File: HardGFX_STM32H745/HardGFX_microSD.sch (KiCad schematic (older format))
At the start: 8 parts, among them J10 PJS008-2003-1

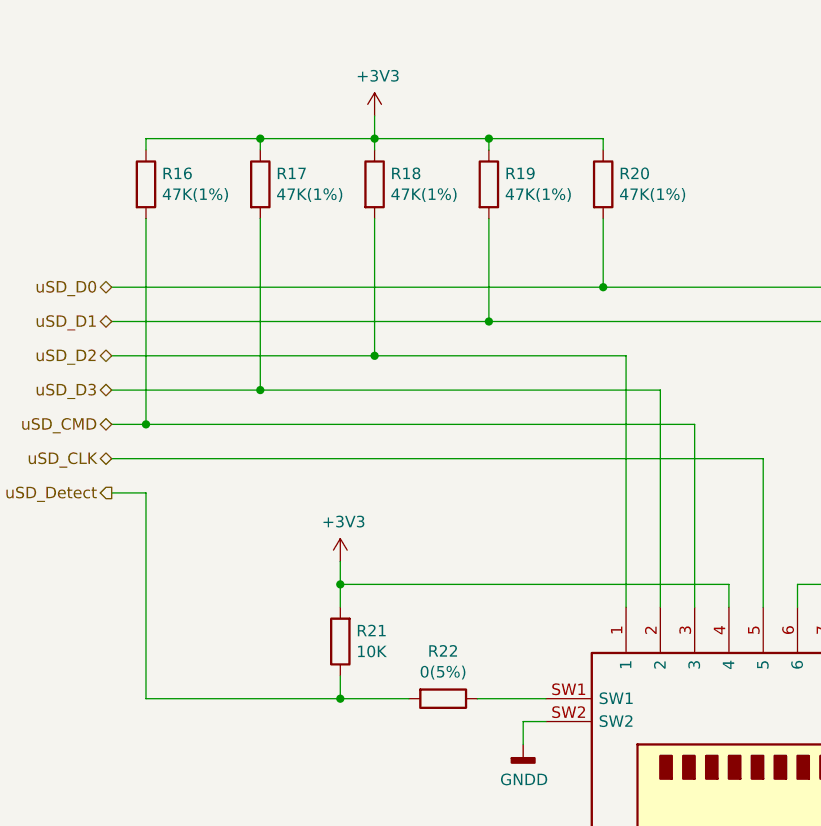
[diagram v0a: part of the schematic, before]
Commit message: Filling field for do BOM with Kicost  and create proyect on IDE to start setting peripheral in MCU
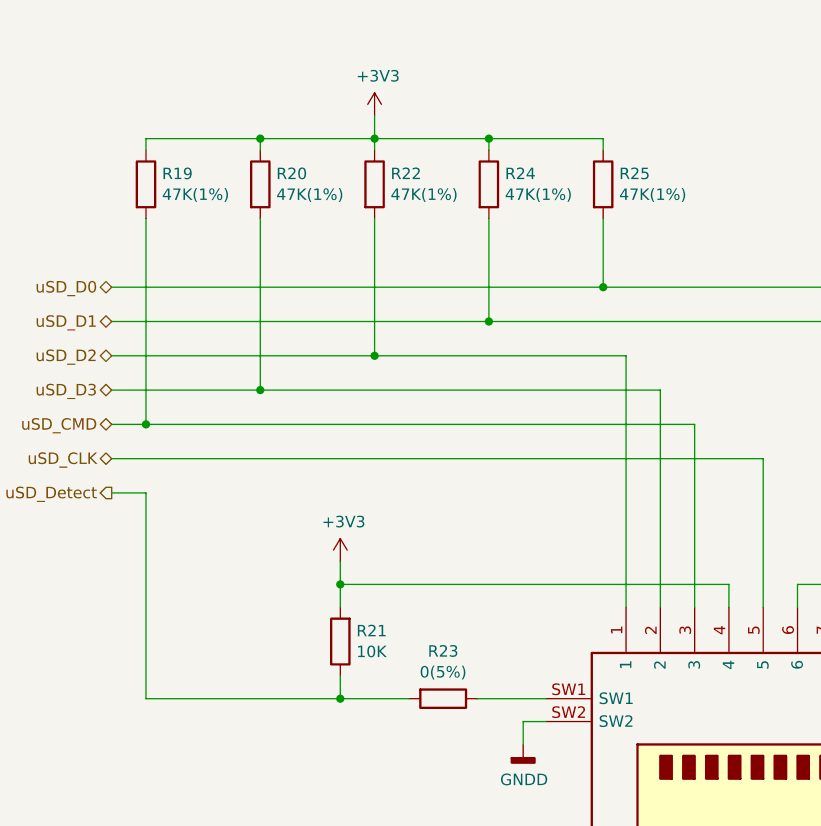
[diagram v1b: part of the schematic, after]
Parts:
- renumbered R16 to R19, R17 to R20, R18 to R22, R22 to R23, R19 to R24, R20 to R25
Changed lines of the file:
@@
 $EndComp
 $Comp
-L power:GNDD #PWR068
+L power:GNDD #PWR080
 U 1 1 60F78B55
 P 5100 6150
-F 0 "#PWR068" H 5100 5900 50  0001 C CNN
+F 0 "#PWR080" H 5100 5900 50  0001 C CNN
 F 1 "GNDD" H 5104 5995 50  0000 C CNN
 F 2 "" H 5100 6150 50  0001 C CNN
@@
 	5100 6050 5100 6150
 $Comp
-L power:GNDD #PWR067
+L power:GNDD #PWR079
 U 1 1 60F79B74
 P 3100 5700
-F 0 "#PWR067" H 3100 5450 50  0001 C CNN
+F 0 "#PWR079" H 3100 5450 50  0001 C CNN
 F 1 "GNDD" H 3104 5545 50  0000 C CNN
 F 2 "" H 3100 5700 50  0001 C CNN
@@
 uSD_D3
 $Comp
-L Device:R R22
+L Device:R R23
 U 1 1 60F7C1AA
 P 2750 5500
-F 0 "R22" V 2543 5500 50  0000 C CNN
+F 0 "R23" V 2543 5500 50  0000 C CNN
 F 1 "0(5%)" V 2634 5500 50  0000 C CNN
 F 2 "" V 2680 5500 50  0001 C CNN
@@
 $EndComp
 $Comp
-L power:+3V3 #PWR065
+L power:+3V3 #PWR077
 U 1 1 60F7DC6F
 P 2300 4900
-F 0 "#PWR065" H 2300 4750 50  0001 C CNN
+F 0 "#PWR077" H 2300 4750 50  0001 C CNN
 F 1 "+3V3" H 2315 5073 50  0000 C CNN
 F 2 "" H 2300 4900 50  0001 C CNN
@@
 $EndComp
 $Comp
-L power:+3V3 #PWR066
+L power:+3V3 #PWR078
 U 1 1 60F7F4C4
 P 2450 2950
-F 0 "#PWR066" H 2450 2800 50  0001 C CNN
+F 0 "#PWR078" H 2450 2800 50  0001 C CNN
 F 1 "+3V3" H 2465 3123 50  0000 C CNN
 F 2 "" H 2450 2950 50  0001 C CNN
@@
 $EndComp
 $Comp
-L Device:R R16
+L Device:R R19
 U 1 1 60F819E6
 P 1450 3250
-F 0 "R16" H 1520 3296 50  0000 L CNN
+F 0 "R19" H 1520 3296 50  0000 L CNN
 F 1 "47K(1%)" H 1520 3205 50  0000 L CNN
 F 2 "" V 1380 3250 50  0001 C CNN
@@
 $EndComp
 $Comp
-L Device:R R17
+L Device:R R20
 U 1 1 60F821A6
 P 1950 3250
-F 0 "R17" H 2020 3296 50  0000 L CNN
+F 0 "R20" H 2020 3296 50  0000 L CNN
 F 1 "47K(1%)" H 2020 3205 50  0000 L CNN
 F 2 "" V 1880 3250 50  0001 C CNN
@@
 $EndComp
 $Comp
-L Device:R R18
+L Device:R R22
 U 1 1 60F8252E
 P 2450 3250
-F 0 "R18" H 2520 3296 50  0000 L CNN
+F 0 "R22" H 2520 3296 50  0000 L CNN
 F 1 "47K(1%)" H 2520 3205 50  0000 L CNN
 F 2 "" V 2380 3250 50  0001 C CNN
@@
 $EndComp
 $Comp
-L Device:R R19
+L Device:R R24
 U 1 1 60F8279F
 P 2950 3250
-F 0 "R19" H 3020 3296 50  0000 L CNN
+F 0 "R24" H 3020 3296 50  0000 L CNN
 F 1 "47K(1%)" H 3020 3205 50  0000 L CNN
 F 2 "" V 2880 3250 50  0001 C CNN
@@
 $EndComp
 $Comp
-L Device:R R20
+L Device:R R25
 U 1 1 60F829CA
 P 3450 3250
-F 0 "R20" H 3520 3296 50  0000 L CNN
+F 0 "R25" H 3520 3296 50  0000 L CNN
 F 1 "47K(1%)" H 3520 3205 50  0000 L CNN
 F 2 "" V 3380 3250 50  0001 C CNN

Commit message: I filled more component to Kicost script
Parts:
- J10: Digikey# (none) -> 2408-PJS008-2003-1TR-ND; MANUFACTURER (none) -> Yamaichi Electronics; Manf# (none) -> PJS008-2003-1; Mouser# (none) -> 945-PJS008-2003-1
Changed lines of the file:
@@
 Sheet 8 8
 Title "microSD"
-Date "2021-06-19"
+Date "2021-08-24"
 Rev "Rev. 1"
 Comp "HardGFX"
@@
 F 2 "PJS008-2003-1:PJS00820031" H 4850 7250 50  0001 L CNN
 F 3 "https://datasheet.ciiva.com/12072/microsd-e-714-12072053.pdf" H 5400 7100 50  0001 L CNN
+F 4 "2408-PJS008-2003-1TR-ND" H 4650 7100 50  0001 C CNN "Digikey#"
+F 5 "Yamaichi Electronics" H 4650 7100 50  0001 C CNN "MANUFACTURER"
+F 6 "PJS008-2003-1" H 4650 7100 50  0001 C CNN "Manf#"
+F 7 "945-PJS008-2003-1" H 4650 7100 50  0001 C CNN "Mouser#"
 	1    4650 7100
 	-1   0    0    1

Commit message: Almost I end to fill Kicost field on schematics.
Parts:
- R19, R20, R22, R24, R25: Digikey# (none) -> 311-47.0KHRCT-ND; MANUFACTURER (none) -> YAGEO; Manf# (none) -> RC0603FR-0747KL; Mouser# (none) -> 603-RC0603FR-0747KL
- R21: Digikey# (none) -> 311-10.0KHRCT-ND; MANUFACTURER (none) -> YAGEO; Manf# (none) -> RC0603FR-0710KL; Mouser# (none) -> 603-RC0603FR-0710KL
- R23: Digikey# (none) -> 311-0.0GRCT-ND; MANUFACTURER (none) -> YAGEO; Manf# (none) -> RC0603JR-070RL; Mouser# (none) -> 603-RC0603JR-070RL
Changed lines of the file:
@@
 Sheet 8 8
 Title "microSD"
-Date "2021-08-24"
+Date "2021-08-25"
 Rev "Rev. 1"
 Comp "HardGFX"
@@
 F 1 "0(5%)" V 2634 5500 50  0000 C CNN
 F 2 "" V 2680 5500 50  0001 C CNN
-F 3 "~" H 2750 5500 50  0001 C CNN
+F 3 "https://www.yageo.com/upload/media/product/productsearch/datasheet/rchip/PYu-RC_Group_51_RoHS_L_11.pdf" H 2750 5500 50  0001 C CNN
+F 4 "311-0.0GRCT-ND" H 2750 5500 50  0001 C CNN "Digikey#"
+F 5 "YAGEO" H 2750 5500 50  0001 C CNN "MANUFACTURER"
+F 6 "RC0603JR-070RL" H 2750 5500 50  0001 C CNN "Manf#"
+F 7 "603-RC0603JR-070RL" H 2750 5500 50  0001 C CNN "Mouser#"
 	1    2750 5500
 	0    1    1    0
@@
 F 1 "10K" H 2230 5295 50  0000 R CNN
 F 2 "" V 2230 5250 50  0001 C CNN
-F 3 "~" H 2300 5250 50  0001 C CNN
+F 3 "https://www.yageo.com/upload/media/product/productsearch/datasheet/rchip/PYu-RC_Group_51_RoHS_L_11.pdf" H 2300 5250 50  0001 C CNN
+F 4 "311-10.0KHRCT-ND" H 2300 5250 50  0001 C CNN "Digikey#"
+F 5 "YAGEO" H 2300 5250 50  0001 C CNN "MANUFACTURER"
+F 6 "RC0603FR-0710KL" H 2300 5250 50  0001 C CNN "Manf#"
+F 7 "603-RC0603FR-0710KL" H 2300 5250 50  0001 C CNN "Mouser#"
 	1    2300 5250
 	-1   0    0    1
@@
 F 1 "47K(1%)" H 1520 3205 50  0000 L CNN
 F 2 "" V 1380 3250 50  0001 C CNN
-F 3 "~" H 1450 3250 50  0001 C CNN
+F 3 "https://www.yageo.com/upload/media/product/productsearch/datasheet/rchip/PYu-RC_Group_51_RoHS_L_11.pdf" H 1450 3250 50  0001 C CNN
+F 4 "311-47.0KHRCT-ND" H 1450 3250 50  0001 C CNN "Digikey#"
+F 5 "YAGEO" H 1450 3250 50  0001 C CNN "MANUFACTURER"
+F 6 "RC0603FR-0747KL" H 1450 3250 50  0001 C CNN "Manf#"
+F 7 "603-RC0603FR-0747KL" H 1450 3250 50  0001 C CNN "Mouser#"
 	1    1450 3250
 	1    0    0    -1
@@
 F 1 "47K(1%)" H 2020 3205 50  0000 L CNN
 F 2 "" V 1880 3250 50  0001 C CNN
-F 3 "~" H 1950 3250 50  0001 C CNN
+F 3 "https://www.yageo.com/upload/media/product/productsearch/datasheet/rchip/PYu-RC_Group_51_RoHS_L_11.pdf" H 1950 3250 50  0001 C CNN
+F 4 "311-47.0KHRCT-ND" H 1950 3250 50  0001 C CNN "Digikey#"
+F 5 "YAGEO" H 1950 3250 50  0001 C CNN "MANUFACTURER"
+F 6 "RC0603FR-0747KL" H 1950 3250 50  0001 C CNN "Manf#"
+F 7 "603-RC0603FR-0747KL" H 1950 3250 50  0001 C CNN "Mouser#"
 	1    1950 3250
 	1    0    0    -1
@@
 F 1 "47K(1%)" H 2520 3205 50  0000 L CNN
 F 2 "" V 2380 3250 50  0001 C CNN
-F 3 "~" H 2450 3250 50  0001 C CNN
+F 3 "https://www.yageo.com/upload/media/product/productsearch/datasheet/rchip/PYu-RC_Group_51_RoHS_L_11.pdf" H 2450 3250 50  0001 C CNN
+F 4 "311-47.0KHRCT-ND" H 2450 3250 50  0001 C CNN "Digikey#"
+F 5 "YAGEO" H 2450 3250 50  0001 C CNN "MANUFACTURER"
+F 6 "RC0603FR-0747KL" H 2450 3250 50  0001 C CNN "Manf#"
+F 7 "603-RC0603FR-0747KL" H 2450 3250 50  0001 C CNN "Mouser#"
 	1    2450 3250
 	1    0    0    -1
@@
 F 1 "47K(1%)" H 3020 3205 50  0000 L CNN
 F 2 "" V 2880 3250 50  0001 C CNN
-F 3 "~" H 2950 3250 50  0001 C CNN
+F 3 "https://www.yageo.com/upload/media/product/productsearch/datasheet/rchip/PYu-RC_Group_51_RoHS_L_11.pdf" H 2950 3250 50  0001 C CNN
+F 4 "311-47.0KHRCT-ND" H 2950 3250 50  0001 C CNN "Digikey#"
+F 5 "YAGEO" H 2950 3250 50  0001 C CNN "MANUFACTURER"
+F 6 "RC0603FR-0747KL" H 2950 3250 50  0001 C CNN "Manf#"
+F 7 "603-RC0603FR-0747KL" H 2950 3250 50  0001 C CNN "Mouser#"
 	1    2950 3250
 	1    0    0    -1
@@
 F 1 "47K(1%)" H 3520 3205 50  0000 L CNN
 F 2 "" V 3380 3250 50  0001 C CNN
-F 3 "~" H 3450 3250 50  0001 C CNN
+F 3 "https://www.yageo.com/upload/media/product/productsearch/datasheet/rchip/PYu-RC_Group_51_RoHS_L_11.pdf" H 3450 3250 50  0001 C CNN
+F 4 "311-47.0KHRCT-ND" H 3450 3250 50  0001 C CNN "Digikey#"
+F 5 "YAGEO" H 3450 3250 50  0001 C CNN "MANUFACTURER"
+F 6 "RC0603FR-0747KL" H 3450 3250 50  0001 C CNN "Manf#"
+F 7 "603-RC0603FR-0747KL" H 3450 3250 50  0001 C CNN "Mouser#"
 	1    3450 3250
 	1    0    0    -1

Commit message: Modified symbols field to use Kicost
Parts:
- J10: Manf# PJS008-2003-1 -> (none); manf# (none) -> PJS008-2003-1
- R19, R20, R22, R24, R25: Manf# RC0603FR-0747KL -> (none); manf# (none) -> RC0603FR-0747KL
- R21: Manf# RC0603FR-0710KL -> (none); manf# (none) -> RC0603FR-0710KL
- R23: Manf# RC0603JR-070RL -> (none); manf# (none) -> RC0603JR-070RL
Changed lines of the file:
@@
 F 4 "2408-PJS008-2003-1TR-ND" H 4650 7100 50  0001 C CNN "Digikey#"
 F 5 "Yamaichi Electronics" H 4650 7100 50  0001 C CNN "MANUFACTURER"
-F 6 "PJS008-2003-1" H 4650 7100 50  0001 C CNN "Manf#"
+F 6 "" H 4650 7100 50  0001 C CNN "Manf#"
 F 7 "945-PJS008-2003-1" H 4650 7100 50  0001 C CNN "Mouser#"
+F 8 "PJS008-2003-1" H 4650 7100 50  0001 C CNN "manf#"
 	1    4650 7100
 	-1   0    0    1
@@
 F 4 "311-0.0GRCT-ND" H 2750 5500 50  0001 C CNN "Digikey#"
 F 5 "YAGEO" H 2750 5500 50  0001 C CNN "MANUFACTURER"
-F 6 "RC0603JR-070RL" H 2750 5500 50  0001 C CNN "Manf#"
+F 6 "" H 2750 5500 50  0001 C CNN "Manf#"
 F 7 "603-RC0603JR-070RL" H 2750 5500 50  0001 C CNN "Mouser#"
+F 8 "RC0603JR-070RL" H 2750 5500 50  0001 C CNN "manf#"
 	1    2750 5500
 	0    1    1    0
@@
 F 4 "311-10.0KHRCT-ND" H 2300 5250 50  0001 C CNN "Digikey#"
 F 5 "YAGEO" H 2300 5250 50  0001 C CNN "MANUFACTURER"
-F 6 "RC0603FR-0710KL" H 2300 5250 50  0001 C CNN "Manf#"
+F 6 "" H 2300 5250 50  0001 C CNN "Manf#"
 F 7 "603-RC0603FR-0710KL" H 2300 5250 50  0001 C CNN "Mouser#"
+F 8 "RC0603FR-0710KL" H 2300 5250 50  0001 C CNN "manf#"
 	1    2300 5250
 	-1   0    0    1
@@
 F 4 "311-47.0KHRCT-ND" H 1450 3250 50  0001 C CNN "Digikey#"
 F 5 "YAGEO" H 1450 3250 50  0001 C CNN "MANUFACTURER"
-F 6 "RC0603FR-0747KL" H 1450 3250 50  0001 C CNN "Manf#"
+F 6 "" H 1450 3250 50  0001 C CNN "Manf#"
 F 7 "603-RC0603FR-0747KL" H 1450 3250 50  0001 C CNN "Mouser#"
+F 8 "RC0603FR-0747KL" H 1450 3250 50  0001 C CNN "manf#"
 	1    1450 3250
 	1    0    0    -1
@@
 F 4 "311-47.0KHRCT-ND" H 1950 3250 50  0001 C CNN "Digikey#"
 F 5 "YAGEO" H 1950 3250 50  0001 C CNN "MANUFACTURER"
-F 6 "RC0603FR-0747KL" H 1950 3250 50  0001 C CNN "Manf#"
+F 6 "" H 1950 3250 50  0001 C CNN "Manf#"
 F 7 "603-RC0603FR-0747KL" H 1950 3250 50  0001 C CNN "Mouser#"
+F 8 "RC0603FR-0747KL" H 1950 3250 50  0001 C CNN "manf#"
 	1    1950 3250
 	1    0    0    -1
@@
 F 4 "311-47.0KHRCT-ND" H 2450 3250 50  0001 C CNN "Digikey#"
 F 5 "YAGEO" H 2450 3250 50  0001 C CNN "MANUFACTURER"
-F 6 "RC0603FR-0747KL" H 2450 3250 50  0001 C CNN "Manf#"
+F 6 "" H 2450 3250 50  0001 C CNN "Manf#"
 F 7 "603-RC0603FR-0747KL" H 2450 3250 50  0001 C CNN "Mouser#"
+F 8 "RC0603FR-0747KL" H 2450 3250 50  0001 C CNN "manf#"
 	1    2450 3250
 	1    0    0    -1
@@
 F 4 "311-47.0KHRCT-ND" H 2950 3250 50  0001 C CNN "Digikey#"
 F 5 "YAGEO" H 2950 3250 50  0001 C CNN "MANUFACTURER"
-F 6 "RC0603FR-0747KL" H 2950 3250 50  0001 C CNN "Manf#"
+F 6 "" H 2950 3250 50  0001 C CNN "Manf#"
 F 7 "603-RC0603FR-0747KL" H 2950 3250 50  0001 C CNN "Mouser#"
+F 8 "RC0603FR-0747KL" H 2950 3250 50  0001 C CNN "manf#"
 	1    2950 3250
 	1    0    0    -1
@@
 F 4 "311-47.0KHRCT-ND" H 3450 3250 50  0001 C CNN "Digikey#"
 F 5 "YAGEO" H 3450 3250 50  0001 C CNN "MANUFACTURER"
-F 6 "RC0603FR-0747KL" H 3450 3250 50  0001 C CNN "Manf#"
+F 6 "" H 3450 3250 50  0001 C CNN "Manf#"
 F 7 "603-RC0603FR-0747KL" H 3450 3250 50  0001 C CNN "Mouser#"
+F 8 "RC0603FR-0747KL" H 3450 3250 50  0001 C CNN "manf#"
 	1    3450 3250
 	1    0    0    -1
